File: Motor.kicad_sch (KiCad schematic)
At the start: 3 parts, among them J3 Screw_Terminal_01x02, J5 Screw_Terminal_01x02, U5 L293D

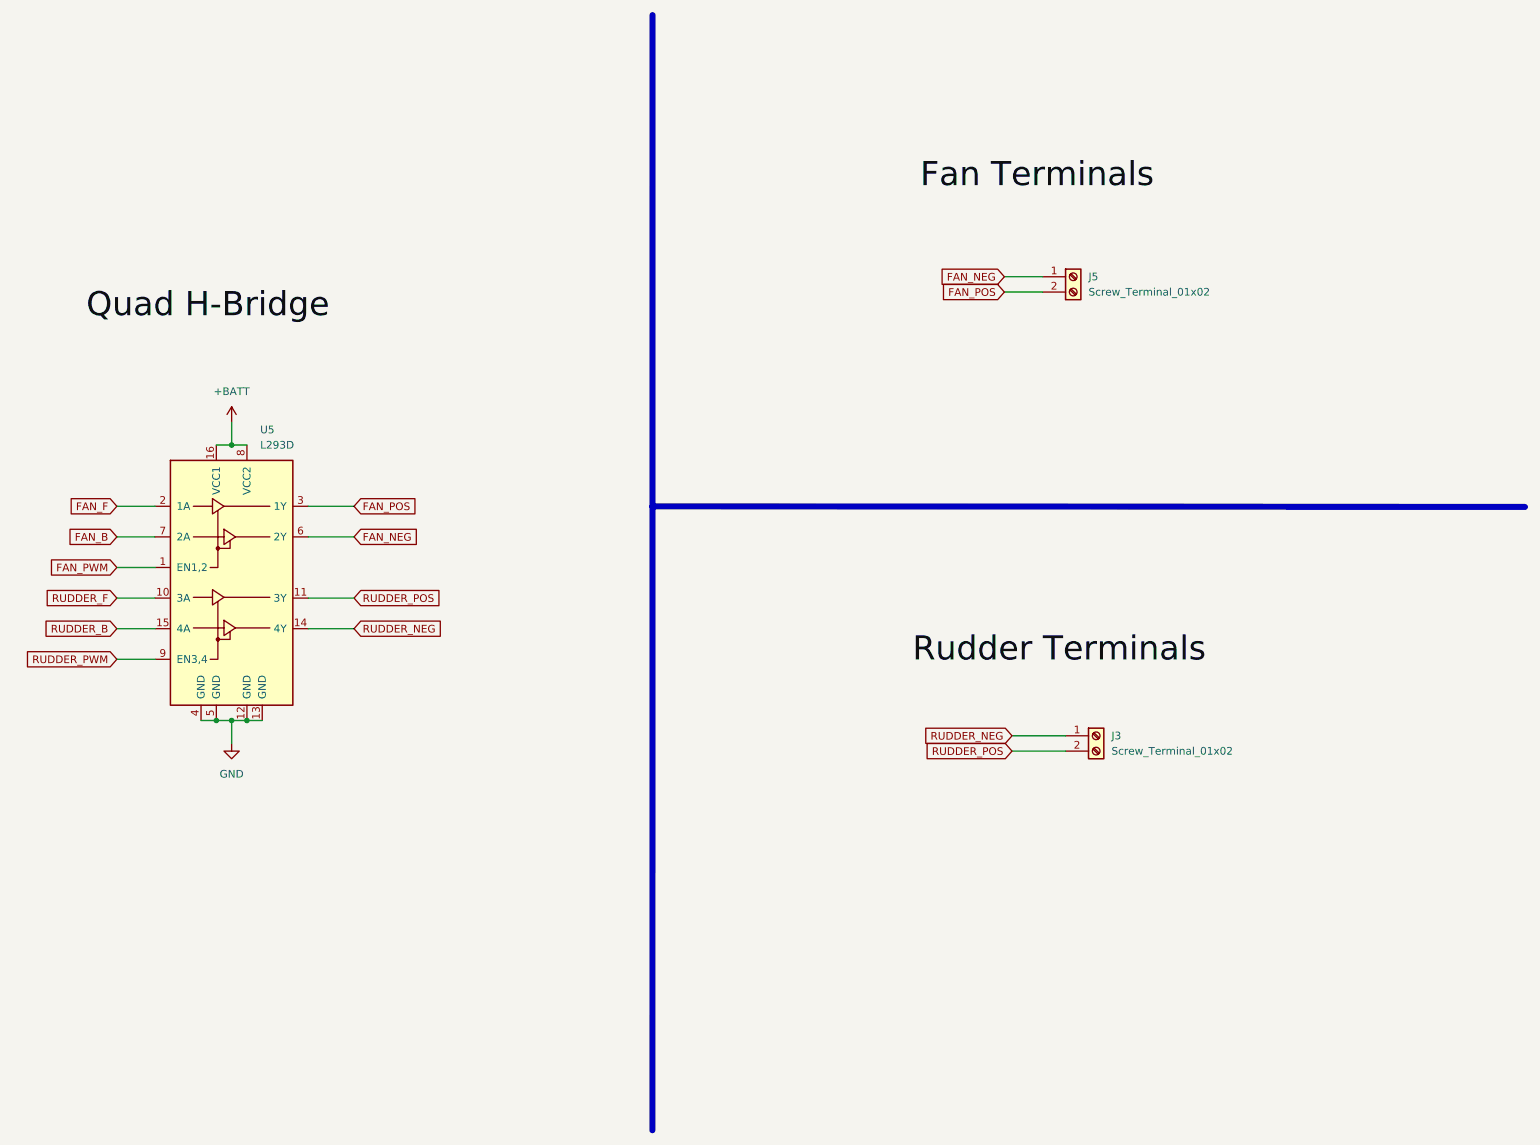
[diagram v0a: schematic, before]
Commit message: Updated PCB to be smaller and support stepper
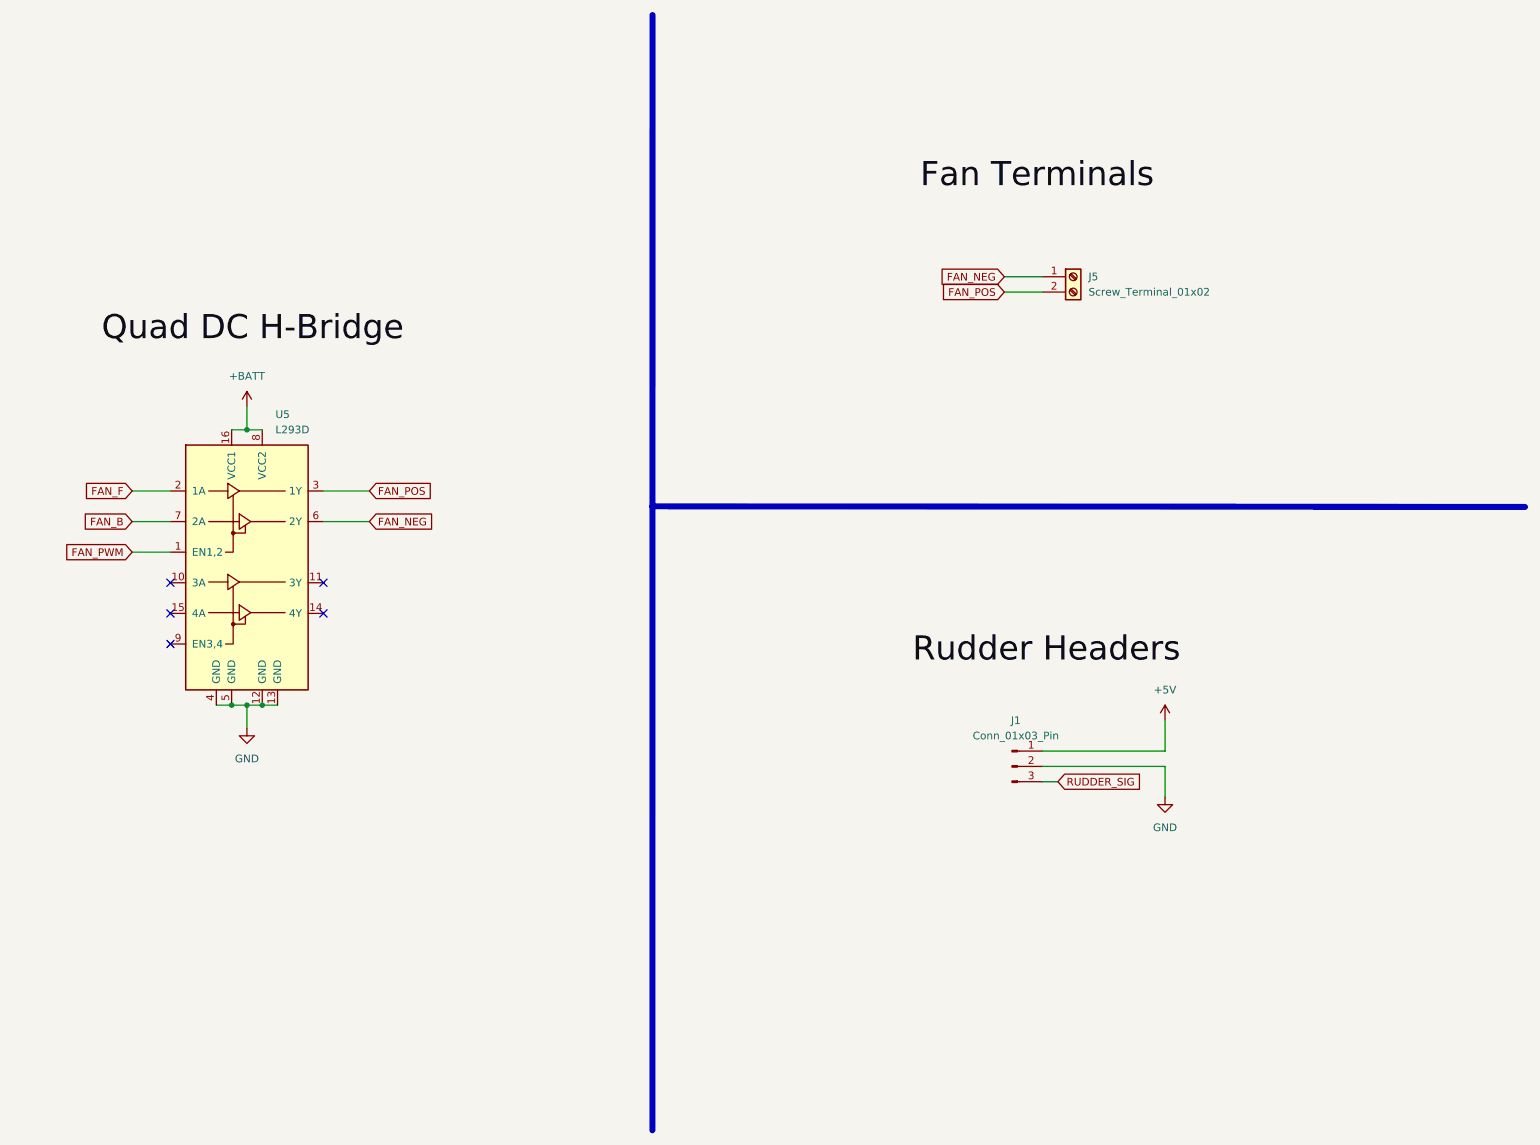
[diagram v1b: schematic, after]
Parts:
- removed J3: Screw_Terminal_01x02, TerminalBlock:TerminalBlock_Altech_AK300-2_P5.00mm, symbol Connector:Screw_Terminal_01x02
- added J1: Conn_01x03_Pin, Connector:FanPinHeader_1x03_P2.54mm_Vertical, symbol Connector:Conn_01x03_Pin
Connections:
- net GND: now also J1.2 (Pin_2)
- net RUDDER_B: no longer names the net of U5.15 (4A)
- net RUDDER_F: no longer names the net of U5.10 (3A)
- net RUDDER_NEG: no longer names the net of U5.14 (4Y)
- net RUDDER_POS: no longer names the net of U5.11 (3Y)
- net RUDDER_PWM: no longer names the net of U5.9 (EN3,4)
- new net +5V: J1.1 (Pin_1)
- new net RUDDER_SIG: J1.3 (Pin_3)
- no-connect marks 0 -> 5
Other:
- moved on the sheet: U5

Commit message: Updated to use boost converters
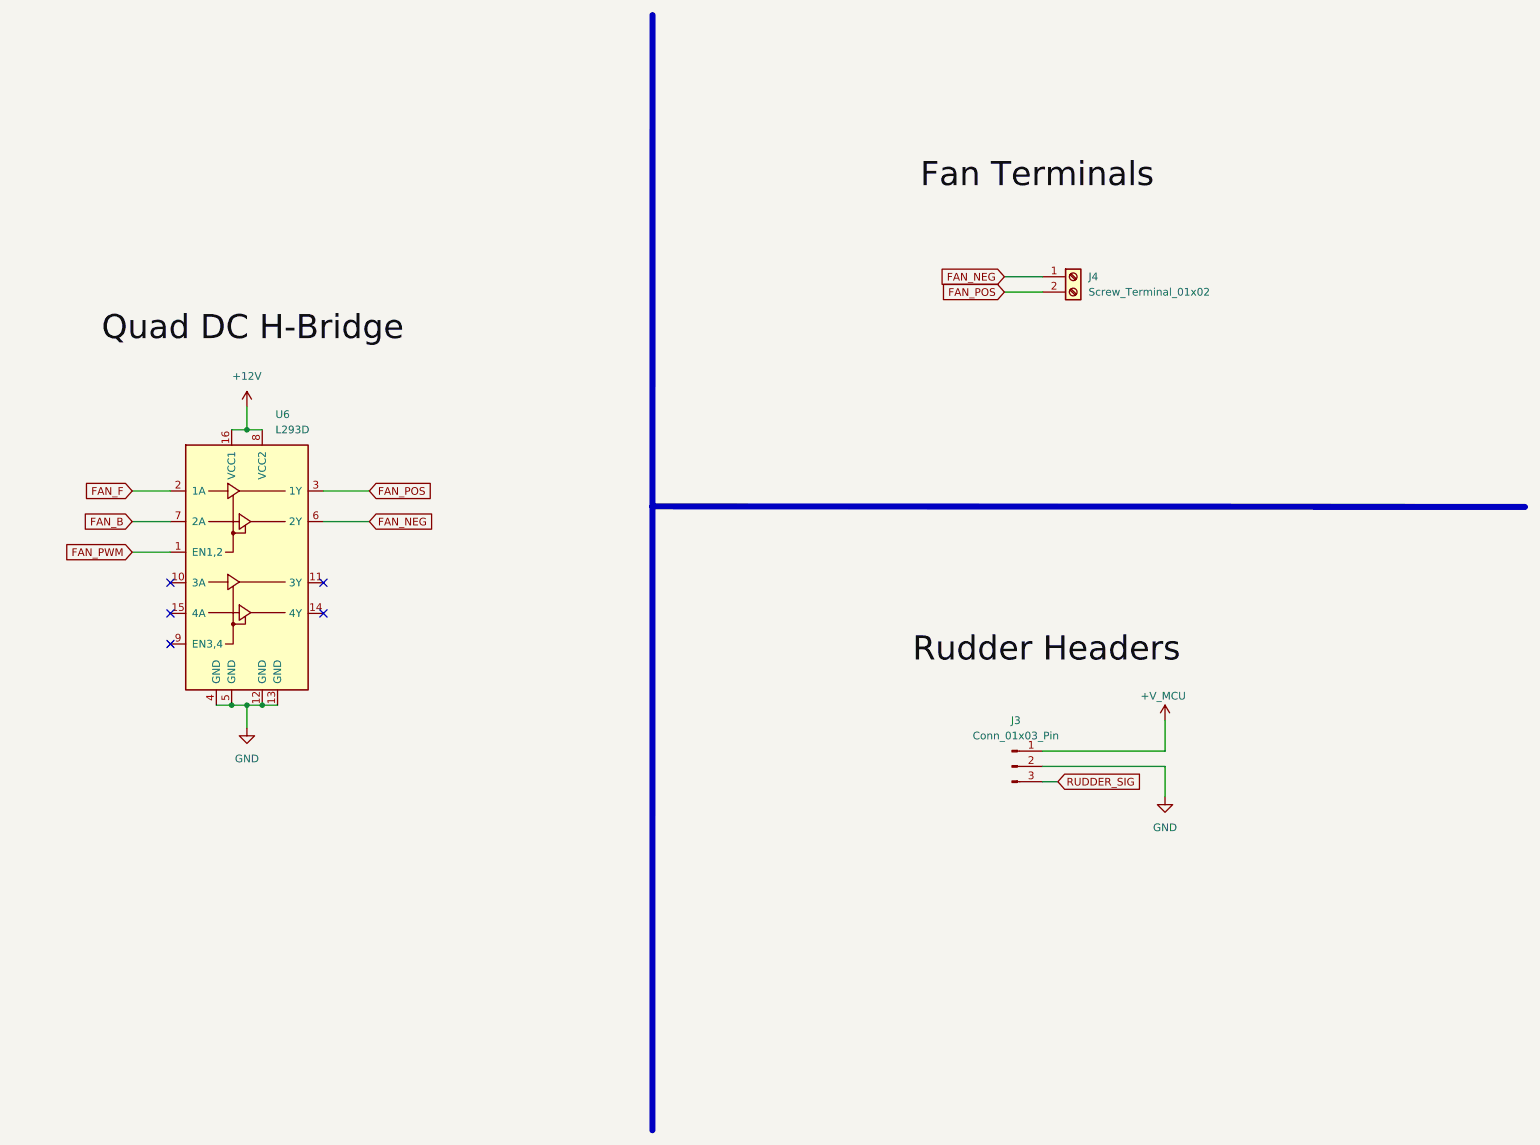
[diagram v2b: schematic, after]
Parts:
- renumbered J1 to J3, J5 to J4, U5 to U6
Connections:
- net +5V renamed +V_MCU
- net +BATT renamed +12V
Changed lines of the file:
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@@
 		(on_board yes)
 		(dnp no)
-		(fields_autoplaced yes)
-		(property "Reference" "#PWR045"
+		(property "Reference" "#PWR049"
 			(at 224.79 133.35 0)
 			(effects
@@
 			)
 		)
-		(property "Value" "+5V"
-			(at 224.79 124.46 0)
-			(effects
-				(font
-					(size 1.27 1.27)
-				)
+		(property "Value" "+V_MCU"
+			(at 220.726 125.476 0)
+			(effects
+				(font
+					(size 1.27 1.27)
+				)
+				(justify left)
 			)
 		)
@@
 			(project "Airboat"
 				(path "/32966cbd-337b-4fa7-b66f-bfe62b1c18c3/b4bf0452-8957-43b4-857b-1edc4fb175d7"
-					(reference "#PWR045")
+					(reference "#PWR049")
 					(unit 1)
 				)
@@
 		(dnp no)
 		(fields_autoplaced yes)
-		(property "Reference" "#PWR030"
+		(property "Reference" "#PWR050"
 			(at 224.79 148.59 0)
 			(effects
@@
 			(project "Airboat"
 				(path "/32966cbd-337b-4fa7-b66f-bfe62b1c18c3/b4bf0452-8957-43b4-857b-1edc4fb175d7"
-					(reference "#PWR030")
+					(reference "#PWR050")
 					(unit 1)
 				)
@@
 		(dnp no)
 		(fields_autoplaced yes)
-		(property "Reference" "U5"
+		(property "Reference" "U6"
 			(at 77.1241 78.74 0)
 			(effects
@@
 			(project "Airboat"
 				(path "/32966cbd-337b-4fa7-b66f-bfe62b1c18c3/b4bf0452-8957-43b4-857b-1edc4fb175d7"
-					(reference "U5")
+					(reference "U6")
+					(unit 1)
+				)
+			)
+		)
+	)
+	(symbol
+		(lib_id "Connector:Screw_Terminal_01x02")
+		(at 209.55 55.88 0)
+		(unit 1)
+		(exclude_from_sim no)
+		(in_bom yes)
+		(on_board yes)
+		(dnp no)
+		(fields_autoplaced yes)
+		(property "Reference" "J4"
+			(at 212.09 55.8799 0)
+			(effects
+				(font
+					(size 1.27 1.27)
+				)
+				(justify left)
+			)
+		)
+		(property "Value" "Screw_Terminal_01x02"
+			(at 212.09 58.4199 0)
+			(effects
+				(font
+					(size 1.27 1.27)
+				)
+				(justify left)
+			)
+		)
+		(property "Footprint" "TerminalBlock:TerminalBlock_Altech_AK300-2_P5.00mm"
+			(at 209.55 55.88 0)
+			(effects
+				(font
+					(size 1.27 1.27)
+				)
+				(hide yes)
+			)
+		)
+		(property "Datasheet" "~"
+			(at 209.55 55.88 0)
+			(effects
+				(font
+					(size 1.27 1.27)
+				)
+				(hide yes)
+			)
+		)
+		(property "Description" "Generic screw terminal, single row, 01x02, script generated (kicad-library-utils/schlib/autogen/connector/)"
+			(at 209.55 55.88 0)
+			(effects
+				(font
+					(size 1.27 1.27)
+				)
+				(hide yes)
+			)
+		)
+		(pin "1"
+		)
+		(pin "2"
+		)
+		(instances
+			(project "Airboat"
+				(path "/32966cbd-337b-4fa7-b66f-bfe62b1c18c3/b4bf0452-8957-43b4-857b-1edc4fb175d7"
+					(reference "J4")
+					(unit 1)
+				)
+			)
+		)
+	)
+	(symbol
+		(lib_id "Connector:Conn_01x03_Pin")
+		(at 199.39 137.16 0)
+		(unit 1)
+		(exclude_from_sim no)
+		(in_bom yes)
+		(on_board yes)
+		(dnp no)
+		(fields_autoplaced yes)
+		(property "Reference" "J3"
+			(at 200.025 129.54 0)
+			(effects
+				(font
+					(size 1.27 1.27)
+				)
+			)
+		)
+		(property "Value" "Conn_01x03_Pin"
+			(at 200.025 132.08 0)
+			(effects
+				(font
+					(size 1.27 1.27)
+				)
+			)
+		)
+		(property "Footprint" "Connector:FanPinHeader_1x03_P2.54mm_Vertical"
+			(at 199.39 137.16 0)
+			(effects
+				(font
+					(size 1.27 1.27)
+				)
+				(hide yes)
+			)
+		)
+		(property "Datasheet" "~"
+			(at 199.39 137.16 0)
+			(effects
+				(font
+					(size 1.27 1.27)
+				)
+				(hide yes)
+			)
+		)
+		(property "Description" "Generic connector, single row, 01x03, script generated"
+			(at 199.39 137.16 0)
+			(effects
+				(font
+					(size 1.27 1.27)
+				)
+				(hide yes)
+			)
+		)
+		(pin "3"
+		)
+		(pin "2"
+		)
+		(pin "1"
+		)
+		(instances
+			(project ""
+				(path "/32966cbd-337b-4fa7-b66f-bfe62b1c18c3/b4bf0452-8957-43b4-857b-1edc4fb175d7"
+					(reference "J3")
 					(unit 1)
 				)
@@
 		(dnp no)
 		(fields_autoplaced yes)
-		(property "Reference" "#PWR041"
+		(property "Reference" "#PWR047"
 			(at 72.39 81.28 0)
 			(effects
@@
 			)
 		)
-		(property "Value" "+BATT"
+		(property "Value" "+12V"
 			(at 72.39 72.39 0)
 			(effects
@@
 			(project "Airboat"
 				(path "/32966cbd-337b-4fa7-b66f-bfe62b1c18c3/b4bf0452-8957-43b4-857b-1edc4fb175d7"
-					(reference "#PWR041")
-					(unit 1)
-				)
-			)
-		)
-	)
-	(symbol
-		(lib_id "Connector:Screw_Terminal_01x02")
-		(at 209.55 55.88 0)
-		(unit 1)
-		(exclude_from_sim no)
-		(in_bom yes)
-		(on_board yes)
-		(dnp no)
-		(fields_autoplaced yes)
-		(property "Reference" "J5"
-			(at 212.09 55.8799 0)
-			(effects
-				(font
-					(size 1.27 1.27)
-				)
-				(justify left)
-			)
-		)
-		(property "Value" "Screw_Terminal_01x02"
-			(at 212.09 58.4199 0)
-			(effects
-				(font
-					(size 1.27 1.27)
-				)
-				(justify left)
-			)
-		)
-		(property "Footprint" "TerminalBlock:TerminalBlock_Altech_AK300-2_P5.00mm"
-			(at 209.55 55.88 0)
-			(effects
-				(font
-					(size 1.27 1.27)
-				)
-				(hide yes)
-			)
-		)
-		(property "Datasheet" "~"
-			(at 209.55 55.88 0)
-			(effects
-				(font
-					(size 1.27 1.27)
-				)
-				(hide yes)
-			)
-		)
-		(property "Description" "Generic screw terminal, single row, 01x02, script generated (kicad-library-utils/schlib/autogen/connector/)"
-			(at 209.55 55.88 0)
-			(effects
-				(font
-					(size 1.27 1.27)
-				)
-				(hide yes)
-			)
-		)
-		(pin "1"
-		)
-		(pin "2"
-		)
-		(instances
-			(project "Airboat"
-				(path "/32966cbd-337b-4fa7-b66f-bfe62b1c18c3/b4bf0452-8957-43b4-857b-1edc4fb175d7"
-					(reference "J5")
-					(unit 1)
-				)
-			)
-		)
-	)
-	(symbol
-		(lib_id "Connector:Conn_01x03_Pin")
-		(at 199.39 137.16 0)
-		(unit 1)
-		(exclude_from_sim no)
-		(in_bom yes)
-		(on_board yes)
-		(dnp no)
-		(fields_autoplaced yes)
-		(property "Reference" "J1"
-			(at 200.025 129.54 0)
-			(effects
-				(font
-					(size 1.27 1.27)
-				)
-			)
-		)
-		(property "Value" "Conn_01x03_Pin"
-			(at 200.025 132.08 0)
-			(effects
-				(font
-					(size 1.27 1.27)
-				)
-			)
-		)
-		(property "Footprint" "Connector:FanPinHeader_1x03_P2.54mm_Vertical"
-			(at 199.39 137.16 0)
-			(effects
-				(font
-					(size 1.27 1.27)
-				)
-				(hide yes)
-			)
-		)
-		(property "Datasheet" "~"
-			(at 199.39 137.16 0)
-			(effects
-				(font
-					(size 1.27 1.27)
-				)
-				(hide yes)
-			)
-		)
-		(property "Description" "Generic connector, single row, 01x03, script generated"
-			(at 199.39 137.16 0)
-			(effects
-				(font
-					(size 1.27 1.27)
-				)
-				(hide yes)
-			)
-		)
-		(pin "3"
-		)
-		(pin "2"
-		)
-		(pin "1"
-		)
-		(instances
-			(project ""
-				(path "/32966cbd-337b-4fa7-b66f-bfe62b1c18c3/b4bf0452-8957-43b4-857b-1edc4fb175d7"
-					(reference "J1")
+					(reference "#PWR047")
 					(unit 1)
 				)
@@
 		(dnp no)
 		(fields_autoplaced yes)
-		(property "Reference" "#PWR040"
+		(property "Reference" "#PWR048"
 			(at 72.39 137.16 0)
 			(effects
@@
 			(project "Airboat"
 				(path "/32966cbd-337b-4fa7-b66f-bfe62b1c18c3/b4bf0452-8957-43b4-857b-1edc4fb175d7"
-					(reference "#PWR040")
-					(unit 1)
-				)
+					(reference "#PWR048")
+					(unit 1)
+				)
